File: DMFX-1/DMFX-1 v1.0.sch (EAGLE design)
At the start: 565 parts, among them IC2 SN74HC4066D, J1 USB-MINIB-5PIN, J1-2 USB-MINIB-5PIN, J10 MONOSW3C, J11 DM3BT-DSF-PEJS, J2 USB-B-SMT, J3 STEREOSW3C, J4 HEADPHONES, J5 87409-110LF, J6 DM3BT-DSF-PEJS, J7 87409-110LF, J8 DCJ0202, J9 MONOSW3C, Q1 MUN2214T1, Q10 MUN2214T1, Q2 MUN2214T1, Q3 MMBF4393, Q4 MUN2214T1, Q5 2N7002ET1G, Q6 2N7002ET1G, Q7 2N7002ET1G, Q8 MUN2214T1, Q9 MUN2214T1, SW1 MB2011SB1W03-DA, SW2 OS102011MA1Q, U10X 24C64SM, U11X TPS73201DBVT, U12X TPS562209SO, U13 741G3157DBVR, U14 ASDM1-12.000MHZ-LC-T, U15X CDCLVC1108PWR, U17 TLV320AIC3204IRHBT, U18 SN74CBTLV3245APW, U19 LME49721, U1X TPS562209SO, U2 AT93C46A-10TQ-2.7, U20 LME49721, U21 LME49721, U22 LME49721, U23 LME49721, U24 LMV358, U3X TPS3803-01DCKR, U4 TMS320C5535, U5 TMS320C5535, U6 FT2232HL, U7 TPD2E001IDRLRQ1, U8 74LVC1G175DBVSOT95, U9 W25Q64FVSFIG, U9-2 W25Q64FVSFIG, Y1 32.768kHz, Y1-2 32.768kHz

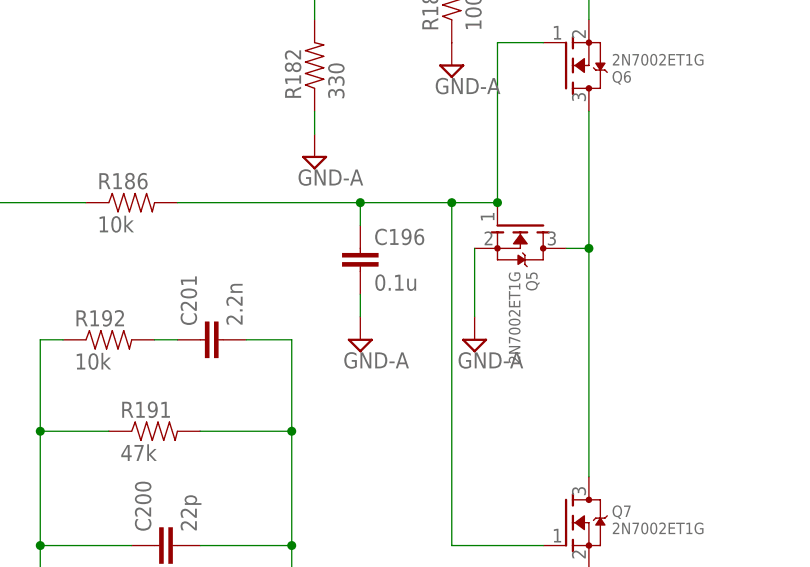
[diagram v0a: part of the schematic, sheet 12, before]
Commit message: 
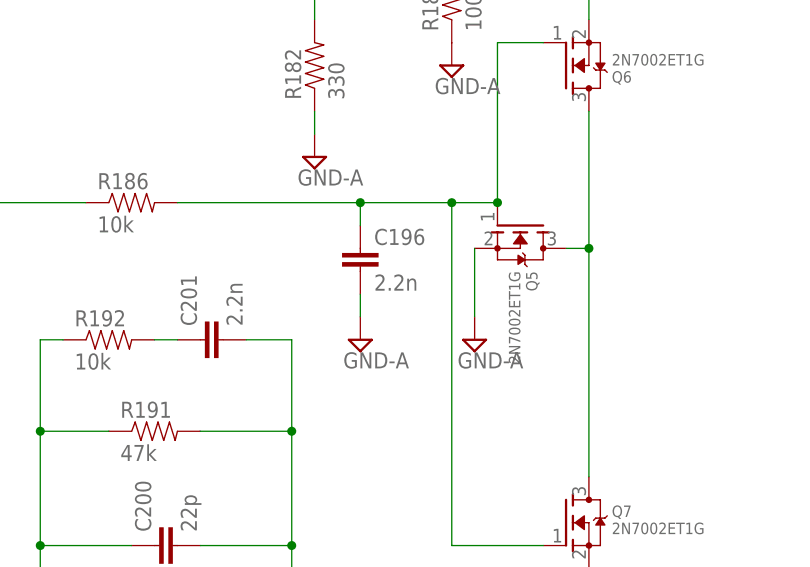
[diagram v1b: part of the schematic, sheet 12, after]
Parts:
- C196: value 0.1u -> 2.2n
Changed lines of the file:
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@@
 <attribute name="MPN" value="2N7002ET1G"/>
 </part>
-<part name="C196" library="SparkFun" deviceset="CAP" device="0402-CAP" value="0.1u">
+<part name="C196" library="SparkFun" deviceset="CAP" device="0402-CAP" value="2.2n">
 <attribute name="MPN" value="GRM155R71H222JA01J"/>
 </part>
